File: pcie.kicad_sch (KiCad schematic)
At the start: 12 parts, among them J8 Conn_01x16_MountingPin

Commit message: Add files via upload
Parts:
- C358: renamed from C105; value 100n -> 1u
- C359: renamed from C106; value 100n -> 1u
- C360: renamed from C107; value 100n -> 1u
- renumbered C104 to C357, J8 to J12, R53 to R148, R54 to R149, R55 to R150, R56 to R151, R57 to R152, R58 to R153, R59 to R154
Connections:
- net PCIe_RESET is gone; now on net PCIE0_RESETn: R152.2
- net PCIe_PWR_EN: now also R148.1
- net PCIE0_WAKEn_M0: now reaches R149.1
- net at R149.2: now also J12.14 (Pin_14)
- net PCIE0_CLKREQn_M0: now reaches R150.1
- net at R150.2: now also J12.15 (Pin_15)
- net PCIE0_RESETn: now reaches R151.1
- net at R151.2: now also J12.16 (Pin_16)
- net at R148.2: now also J12.13 (Pin_13)
- net +5V renamed VCC5V0_SYS
- net PCIe_CLK_N renamed PCIE0_REFCLK_N
- net PCIe_CLK_P renamed PCIE0_REFCLK_P
- net PCIe_RX_N renamed PCIE0_RX_N
- net PCIe_RX_P renamed PCIE0_RX_P
- net PCIe_TX_N renamed PCIE0_TX_N
- net PCIe_TX_P renamed PCIE0_TX_P
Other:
- moved on the sheet: C357, C358, C359, C360, J12, R148, R149, R150, R151, R152, R153, R154

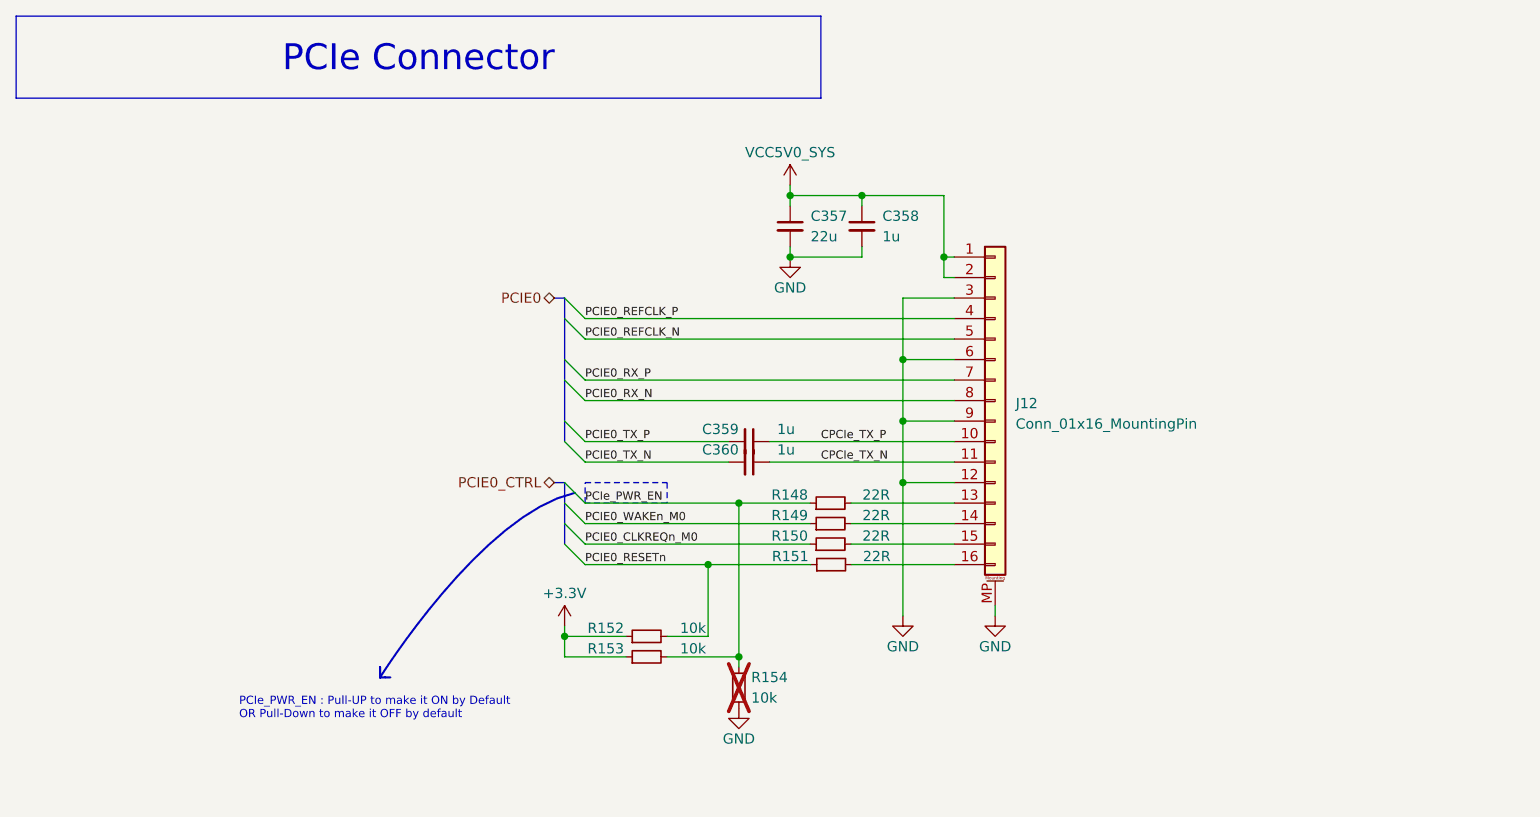
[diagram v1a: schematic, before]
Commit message: SBC Board V0.2
The SBC schematics before footprint and part number check
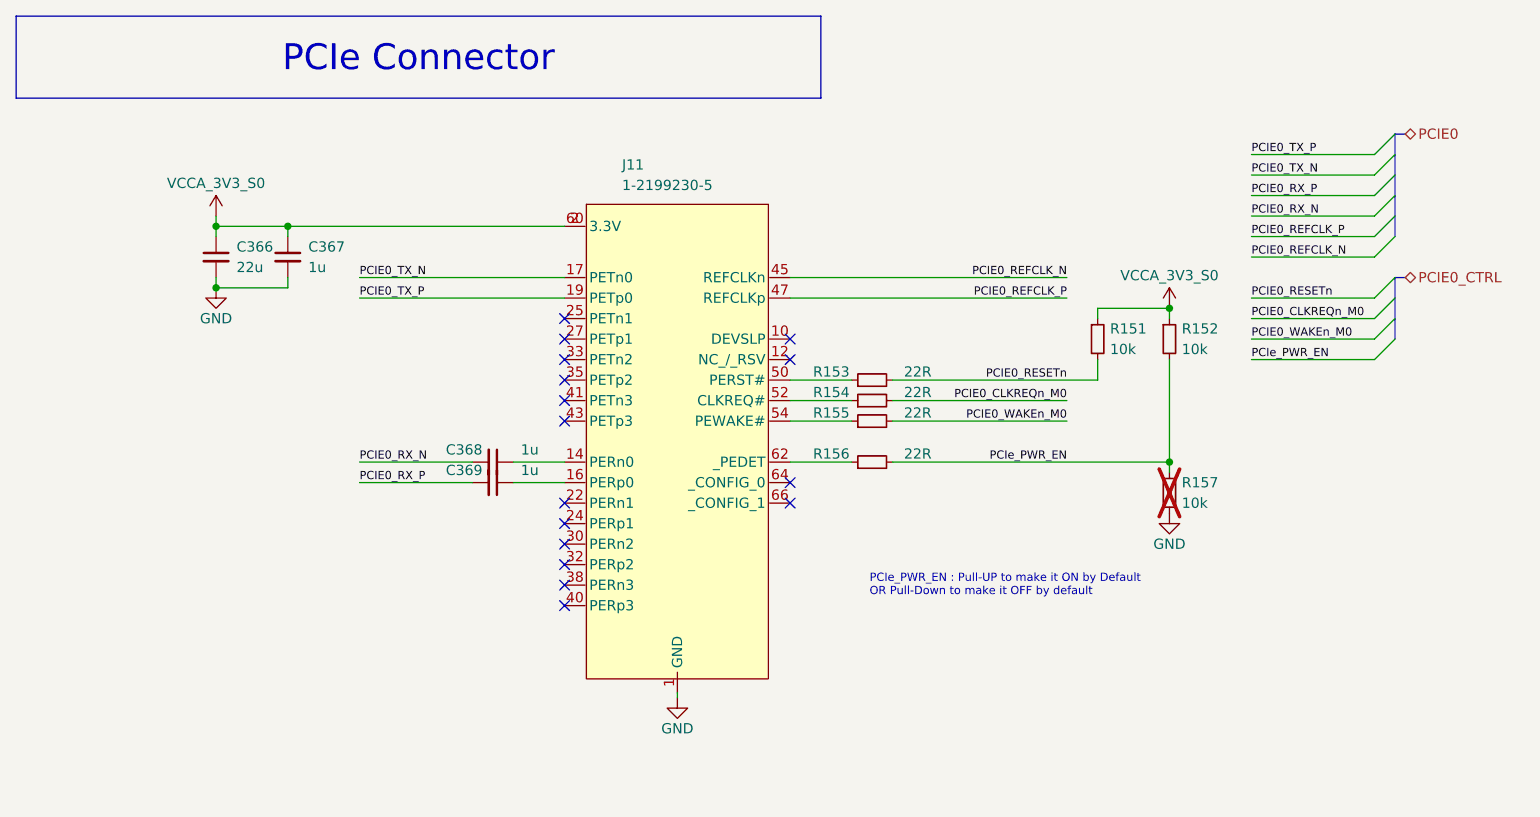
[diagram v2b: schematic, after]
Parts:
- removed C357: 22u, Capacitor_SMD:C_0603_1608Metric, symbol New_Library_0:C_Small_edited
- removed C358, C359, C360: 1u, Capacitor_SMD:C_0201_0603Metric_Pad0.64x0.40mm_HandSolder, symbol New_Library_0:C_Small_edited
- removed J12: Conn_01x16_MountingPin, symbol Connector_Generic_MountingPin:Conn_01x16_MountingPin
- removed R148, R149, R150: 22R, PCM_Resistor_SMD_AKL:R_0402_1005Metric, symbol Device:R_Small
- added C366: 22u, Capacitor_SMD:C_0603_1608Metric, symbol New_Library_0:C_Small_edited
- added C367, C368, C369: 1u, Capacitor_SMD:C_0201_0603Metric_Pad0.64x0.40mm_HandSolder, symbol New_Library_0:C_Small_edited
- added J11: 1-2199230-5, easyeda2kicad:PCIE-SMD_75P-P0.50_1-2199230-5, symbol easyeda2kicad:1-2199230-5
- added R155, R156: 22R, PCM_Resistor_SMD_AKL:R_0402_1005Metric, symbol Device:R_Small
- added R157: 10k, PCM_Resistor_SMD_AKL:R_0402_1005Metric, symbol Device:R_Small
- R151: value 22R -> 10k
- R153: value 10k -> 22R
- R154: value 10k -> 22R; now fitted
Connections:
- net GND: now also C366.2, C367.2, J11.1 (GND), J11.11 (GND), J11.13 (GND), J11.15 (GND), J11.18 (GND), J11.20 (GND), J11.21 (GND), J11.23 (GND), J11.26 (GND), J11.28 (GND), J11.29 (GND), J11.3 (GND), J11.31 (GND), J11.34 (GND), J11.36 (GND), J11.37 (GND), J11.39 (GND), J11.42 (GND), J11.44 (GND), J11.46 (GND), J11.48 (GND), J11.49 (GND), J11.5 (GND), J11.51 (GND), J11.53 (GND), J11.55 (GND), J11.57 (GND), J11.59 (GND), J11.61 (GND), J11.63 (GND), J11.65 (GND), J11.7 (GND), J11.9 (GND), R157.2; no longer R154.2
- net PCIE0_CLKREQn_M0: now also R154.2
- net PCIE0_REFCLK_N: now also J11.45 (REFCLKn)
- net PCIE0_REFCLK_P: now also J11.47 (REFCLKp)
- net PCIE0_RESETn: now also R151.2, R153.2; no longer R151.1, R152.2
- net PCIE0_RX_N: now also C368.2
- net PCIE0_RX_P: now also C369.2
- net PCIE0_TX_N: now also J11.17 (PETn0)
- net PCIE0_TX_P: now also J11.19 (PETp0)
- net PCIE0_WAKEn_M0: now also R155.2
- net PCIe_PWR_EN: now also R152.2, R156.2, R157.1; no longer R153.2, R154.1
- net +3.3V: no longer names the net of R153.1
- net +3.3V: now also J11.50 (PERST#); no longer R152.1
- new net: J11.54 (PEWAKE#), R155.1
- new net: J11.62 (_PEDET), R156.1
- new net: C368.1, J11.14 (PERn0)
- new net: C369.1, J11.16 (PERp0)
- new net: J11.52 (CLKREQ#), R154.1
- new net VCCA_3V3_S0: C366.1, C367.1, J11.2 (3.3V), J11.4 (3.3V), J11.56 (3.3V), J11.58 (3.3V), J11.6 (3.3V), J11.60 (3.3V), J11.8 (3.3V), R151.1, R152.1
- no-connect marks 0 -> 16

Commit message: SBCv0.3
there is no big thing update just some LCSC & Mouser parts
and Big problem deleted alot of component values (:
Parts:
- C366: LCSC Part (none) -> C86295; Mouser Part (none) -> CL10A226MP8NUNE
- C367, C368, C369: LCSC Part (none) -> C5209398; Mouser Part (none) -> CL03A105KP3NSNC
- J11: Mouser Part (none) -> 571-1-2199230-5
- R151, R152: LCSC Part (none) -> (at 0 0 0)
- R153, R154, R155, R156: value 22R -> (none); LCSC Part (none) -> (do_not_autoplace no)
- R157: value 10k -> (none); Mouser Part (none) -> (font (size 1.27 1.27))

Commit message: SBCv0.4
add LCSC & Mouser parts 
and solve the deleted value in the past version
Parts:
- R151, R152: LCSC Part (at 0 0 0) -> C60490; Mouser Part (none) -> 603-RC0402FR-0710KL
- R153, R154, R155, R156: value (none) -> 22R; LCSC Part (do_not_autoplace no) -> C114765; Mouser Part (none) -> 603-RC0402FR-0722RL
- R157: value (none) -> 10k; LCSC Part (none) -> C60490; Mouser Part (font (size 1.27 1.27)) -> 603-RC0402FR-0710KL
